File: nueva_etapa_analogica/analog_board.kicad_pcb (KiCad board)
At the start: 2 copper layers, 36.6 x 44.5 mm, 44 parts, among them J101 Conn_01x02, J102 Conn_01x03, J103 Conn_01x03, J104 Conn_01x03, J105 Conn_01x03, J106 Conn_01x03, J107 Conn_01x03, J108 Conn_01x03, J109 Conn_01x03, J110 Conn_01x03, J111 Conn_01x02, U101 MAX4522CSE+, U102 TLV3544, U103 CPC1017N, U104 CPC1017N, U105 CPC1017N, U106 CPC1017N

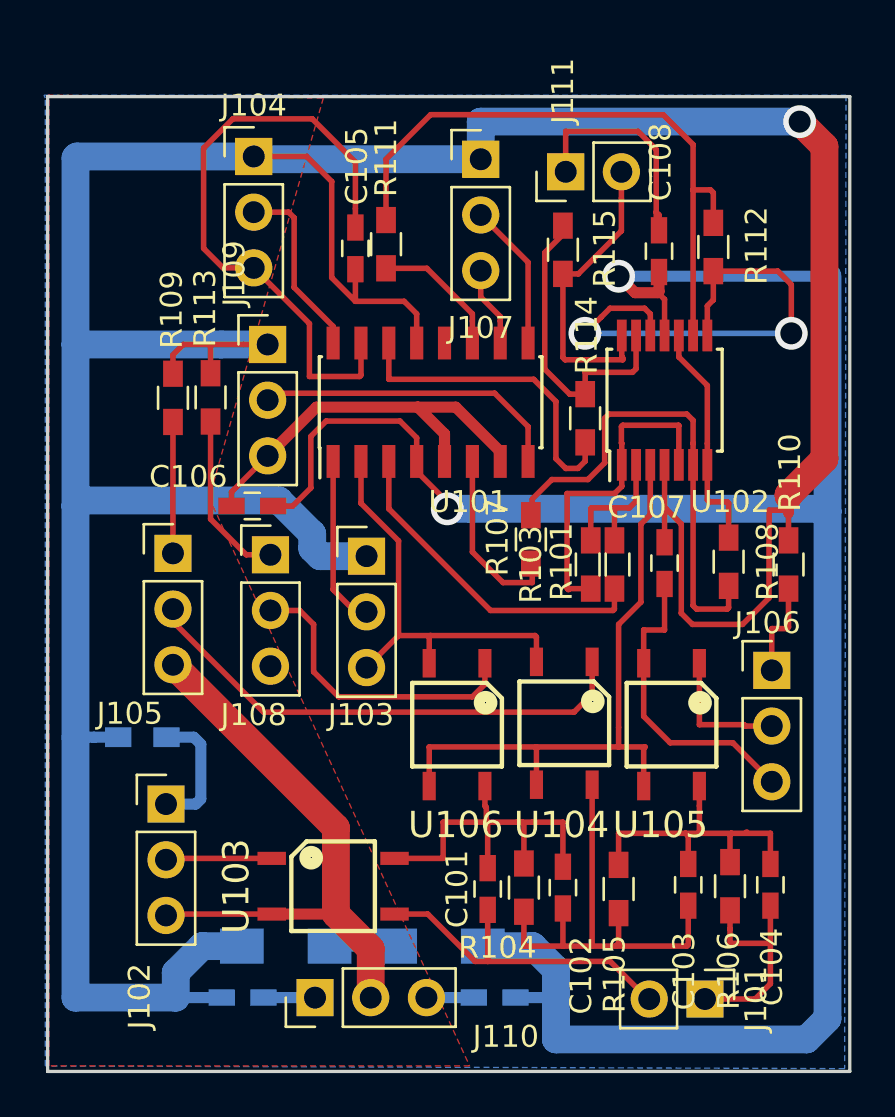
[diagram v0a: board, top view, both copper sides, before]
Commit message: New version of mainboard. Corrected errors and modified analog part.
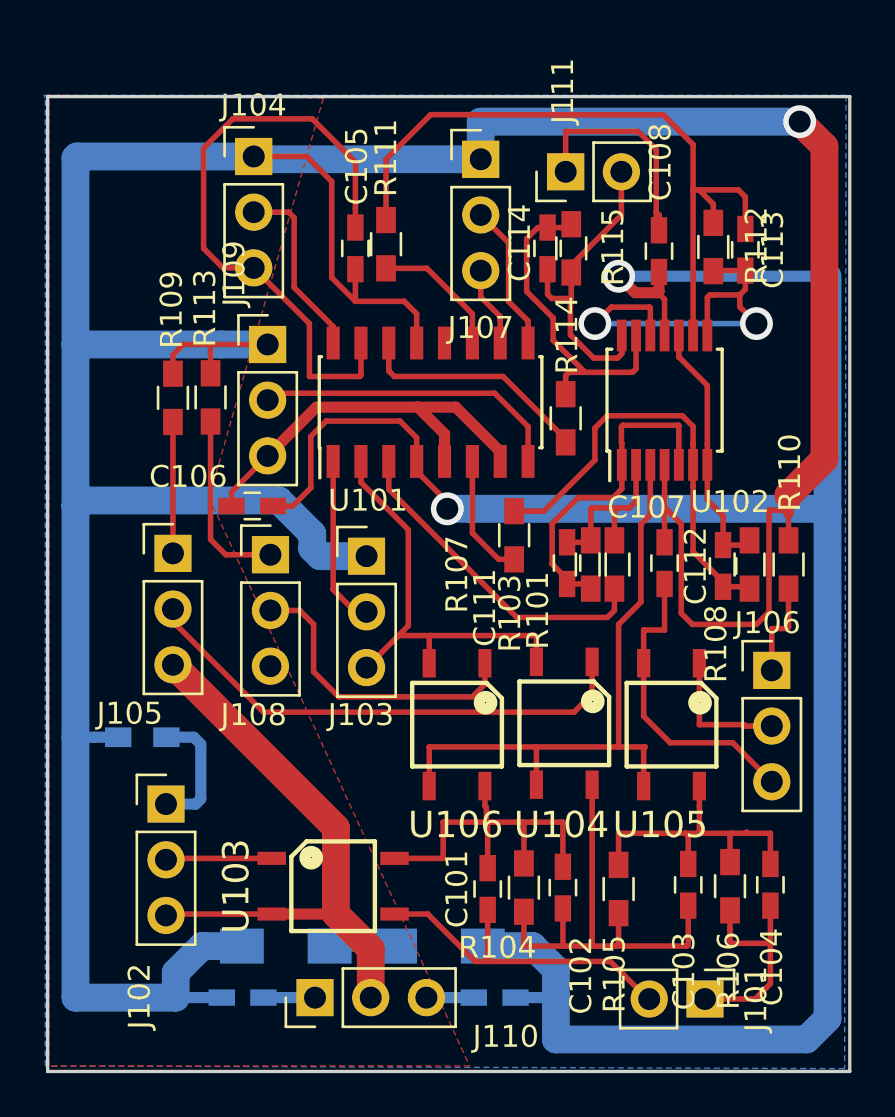
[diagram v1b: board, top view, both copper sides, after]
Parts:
- added C111: 10pF, Capacitors_SMD:C_0603_HandSoldering, F.Cu at (132.9, 92.9)
- added C112: 10pF, Capacitors_SMD:C_0603_HandSoldering, F.Cu at (140.0, 93.0)
- added C113: 10pF, Capacitors_SMD:C_0603_HandSoldering, F.Cu at (141.0, 78.6)
- added C114: 10pF, Capacitors_SMD:C_0603_HandSoldering, F.Cu at (132.0, 78.5)
- moved R108 0.96 mm to (141.2, 93.0)
- moved R114 0.89 mm to (132.8, 86.3)
- moved R107 0.79 mm to (130.5, 91.6)
- moved R115 0.39 mm to (133.1, 78.5)
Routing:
- net Net-(R114-Pad1): track 14.8 -> 10.8 mm
- net Net-(C113-Pad2): track 23.0 -> 19.0 mm
- net Net-(C113-Pad1): track 29.3 -> 32.7 mm
- net Net-(R107-Pad1): track 8.69 -> 5.67 mm
- net Net-(C112-Pad1): track 21.8 -> 20.1 mm
- net Net-(C111-Pad1): track 6.79 -> 7.90 mm
- net Net-(C114-Pad1): track 14.1 -> 15.2 mm
- net Net-(C112-Pad2): track 10.6 -> 11.7 mm
- net Net-(J108-Pad1): track 7.85 -> 8.40 mm
- net Net-(C114-Pad2): track 13.9 -> 14.4 mm
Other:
- net class Default: clearance 0.127 -> 0.1778; trace_width 0.127 -> 0.1778
- rule trace_clearance: 0.127 -> 0.1778

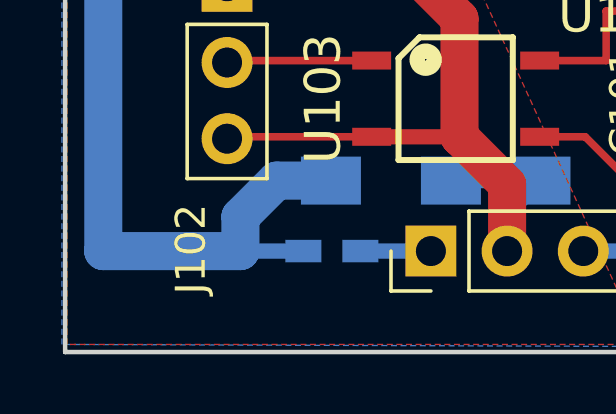
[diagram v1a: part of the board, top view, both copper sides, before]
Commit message: no copper in holes, labels to indicate front and bottom
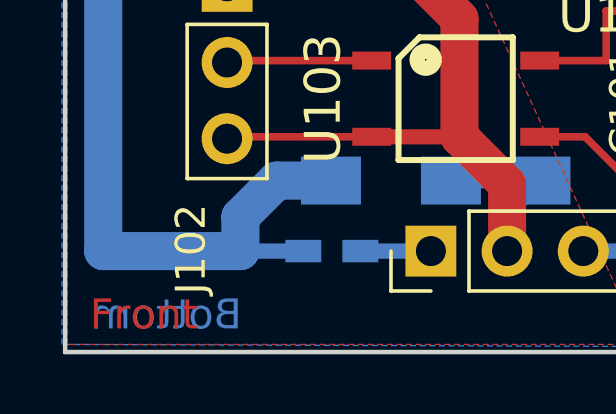
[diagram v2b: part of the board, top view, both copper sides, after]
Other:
- board text added: "Bottom"
- board text added: "Front"
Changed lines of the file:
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@@
-(kicad_pcb (version 4) (host pcbnew 4.0.7-e2-6376~58~ubuntu16.04.1)
+(kicad_pcb (version 20170123) (host pcbnew no-vcs-found-7625~57~ubuntu14.04.1)
   (general
     (links 104)
     (no_connects 0)
-    (area 109.048563 69.386676 149.862586 117.501419)
+    (area 109.048563 69.311676 149.962586 117.576419)
     (thickness 1.6)
-    (drawings 9)
+    (drawings 11)
     (tracks 393)
     (zones 0)
@@
     (47 F.CrtYd user hide)
     (48 B.Fab user hide)
-    (49 F.Fab user hide)
+    (49 F.Fab user)
   )
   (setup
-    (last_trace_width 0.254)
+    (last_trace_width 0.1778)
     (user_trace_width 0.127)
     (user_trace_width 0.254)
@@
     (visible_elements FFFFFF7F)
     (pcbplotparams
-      (layerselection 0x00000_80000000)
+      (layerselection 0x00000_ffffffff)
       (usegerberextensions false)
       (excludeedgelayer true)
@@
       (hpglpenspeed 20)
       (hpglpendiameter 15)
-      (hpglpenoverlay 2)
-      (psnegative true)
+      (psnegative false)
       (psa4output false)
       (plotreference false)
@@
       (outputformat 5)
       (mirror false)
-      (drillshape 0)
+      (drillshape 2)
       (scaleselection 1)
-      (outputdirectory ""))
+      (outputdirectory output/))
   )
   (net 0 "")
@@
     (fp_line (start 1.8 4.35) (end 1.8 -1.8) (layer F.CrtYd) (width 0.05))
     (fp_line (start 1.8 -1.8) (end -1.8 -1.8) (layer F.CrtYd) (width 0.05))
-    (fp_text user %R (at 0 1.27 360) (layer F.Fab)
+    (fp_text user %R (at 0 1.27) (layer F.Fab)
       (effects (font (size 1 1) (thickness 0.15)))
     )
@@
     (tags "capacitor 0603")
     (attr smd)
-    (fp_text reference C107 (at -2.54 0.8255 360) (layer F.SilkS)
+    (fp_text reference C107 (at -2.54 0.8255) (layer F.SilkS)
       (effects (font (size 1 1) (thickness 0.15)))
     )
@@
       (rotate (xyz 0 0 0))
     )
+  )
+  (gr_text Bottom (at 112.593 114.828) (layer B.Cu)
+    (effects (font (size 1 1) (thickness 0.2)) (justify mirror))
+  )
+  (gr_text Front (at 111.843 114.828) (layer F.Cu)
+    (effects (font (size 1 1) (thickness 0.2)))
   )
   (gr_line (start 145.796 116.078) (end 145.796 71.628) (angle 90) (layer Edge.Cuts) (width 0.15))
@@
   (segment (start 119.4375 106.3625) (end 114.681 106.3625) (width 0.254) (layer F.Cu) (net 7))
   (segment (start 114.681 106.3625) (end 114.6175 106.426) (width 0.254) (layer F.Cu) (net 7))
+  (segment (start 115.062 111.5695) (end 115.062 112.7125) (width 1.27) (layer B.Cu) (net 8))
   (segment (start 137.3505 90.424) (end 137.414 90.424) (width 0.254) (layer F.Cu) (net 8))
   (segment (start 138.1125 95.1865) (end 138.6205 95.6945) (width 0.254) (layer F.Cu) (net 8))
@@
   (segment (start 118.0785 110.363) (end 116.2685 110.363) (width 1.27) (layer B.Cu) (net 8))
   (segment (start 116.2685 110.363) (end 115.062 111.5695) (width 1.27) (layer B.Cu) (net 8))
-  (segment (start 115.062 111.5695) (end 115.062 112.7125) (width 1.27) (layer B.Cu) (net 8))
   (segment (start 117.16 112.7125) (end 115.062 112.7125) (width 0.508) (layer B.Cu) (net 8))
   (segment (start 128.9685 74.4855) (end 118.745 74.4855) (width 1.27) (layer B.Cu) (net 8))
@@
     (polygon
       (pts
-        (xy 109.22 71.5645) (xy 121.793 71.6915) (xy 116.586 89.916) (xy 128.4605 115.824) (xy 109.2835 115.824)
-        (xy 109.2835 71.6915) (xy 109.2835 71.6915)
+        (xy 121.793 71.6915) (xy 116.586 89.916) (xy 128.4605 115.824) (xy 109.2835 115.824) (xy 109.2835 71.6915)
+        (xy 109.22 71.5645)
       )
     )
@@
       )
     )
+  )
+  (zone (net 0) (net_name "") (layer F.Cu) (hatch edge 0.508)
+    (connect_pads (clearance 0.508))
+    (min_thickness 0.254)
+    (keepout (tracks not_allowed) (vias not_allowed) (copperpour not_allowed))
+    (fill (arc_segments 16) (thermal_gap 0.508) (thermal_bridge_width 0.508))
+    (polygon
+      (pts
+        (xy 109.843 114.078) (xy 114.093 114.078) (xy 114.093 115.578) (xy 109.843 115.578)
+      )
+    )
+  )
+  (zone (net 0) (net_name "") (layer B.Cu) (hatch edge 0.508)
+    (connect_pads (clearance 0.508))
+    (min_thickness 0.254)
+    (keepout (tracks not_allowed) (vias not_allowed) (copperpour not_allowed))
+    (fill (arc_segments 16) (thermal_gap 0.508) (thermal_bridge_width 0.508))
+    (polygon
+      (pts
+        (xy 109.843 115.578) (xy 115.343 115.578) (xy 115.343 114.078) (xy 109.843 114.078)
+      )
+    )
